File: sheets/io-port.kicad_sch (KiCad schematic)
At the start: 3 parts, among them J2 Conn_02x05_Odd_Even, U8 PCF8574AT

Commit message: add mcu module + position components
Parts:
- SW2: value ~ -> TDS08SGRNTU04; footprint (none) -> Connectors:TDS08SGRNTU04; LCSC (none) -> C6284382
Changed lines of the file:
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@@
 		(on_board yes)
 		(dnp no)
-		(property "Reference" "#PWR042"
+		(property "Reference" "#PWR043"
 			(at 203.2 53.34 0)
 			(effects
@@
 			(project "esp32-didatic-kit"
 				(path "/f57920a5-fee7-4fe5-a133-e8b36941a5a6/9698fb71-dcf7-48f9-beeb-6e6a219382b5/5496c104-71a9-407f-b983-09bd756c4ea4"
-					(reference "#PWR076")
-					(unit 1)
-				)
-				(path "/f57920a5-fee7-4fe5-a133-e8b36941a5a6/9698fb71-dcf7-48f9-beeb-6e6a219382b5/6574d7d9-6af9-409e-b5ea-1bf318741d30"
-					(reference "#PWR070")
-					(unit 1)
-				)
-				(path "/f57920a5-fee7-4fe5-a133-e8b36941a5a6/9698fb71-dcf7-48f9-beeb-6e6a219382b5/8379860e-8981-4170-acaa-d64afdf257d5"
-					(reference "#PWR042")
-					(unit 1)
-				)
-				(path "/f57920a5-fee7-4fe5-a133-e8b36941a5a6/9698fb71-dcf7-48f9-beeb-6e6a219382b5/ecc54a16-e833-4b48-9402-1bdf868c1d08"
-					(reference "#PWR064")
+					(reference "#PWR077")
+					(unit 1)
+				)
+				(path "/f57920a5-fee7-4fe5-a133-e8b36941a5a6/9698fb71-dcf7-48f9-beeb-6e6a219382b5/6574d7d9-6af9-409e-b5ea-1bf318741d30"
+					(reference "#PWR071")
+					(unit 1)
+				)
+				(path "/f57920a5-fee7-4fe5-a133-e8b36941a5a6/9698fb71-dcf7-48f9-beeb-6e6a219382b5/8379860e-8981-4170-acaa-d64afdf257d5"
+					(reference "#PWR043")
+					(unit 1)
+				)
+				(path "/f57920a5-fee7-4fe5-a133-e8b36941a5a6/9698fb71-dcf7-48f9-beeb-6e6a219382b5/ecc54a16-e833-4b48-9402-1bdf868c1d08"
+					(reference "#PWR065")
 					(unit 1)
 				)
@@
 		(dnp no)
 		(fields_autoplaced yes)
-		(property "Reference" "#PWR041"
+		(property "Reference" "#PWR042"
 			(at 153.67 91.44 0)
 			(effects
@@
 			(project "esp32-didatic-kit"
 				(path "/f57920a5-fee7-4fe5-a133-e8b36941a5a6/9698fb71-dcf7-48f9-beeb-6e6a219382b5/5496c104-71a9-407f-b983-09bd756c4ea4"
-					(reference "#PWR075")
-					(unit 1)
-				)
-				(path "/f57920a5-fee7-4fe5-a133-e8b36941a5a6/9698fb71-dcf7-48f9-beeb-6e6a219382b5/6574d7d9-6af9-409e-b5ea-1bf318741d30"
-					(reference "#PWR069")
-					(unit 1)
-				)
-				(path "/f57920a5-fee7-4fe5-a133-e8b36941a5a6/9698fb71-dcf7-48f9-beeb-6e6a219382b5/8379860e-8981-4170-acaa-d64afdf257d5"
-					(reference "#PWR041")
-					(unit 1)
-				)
-				(path "/f57920a5-fee7-4fe5-a133-e8b36941a5a6/9698fb71-dcf7-48f9-beeb-6e6a219382b5/ecc54a16-e833-4b48-9402-1bdf868c1d08"
-					(reference "#PWR063")
+					(reference "#PWR076")
+					(unit 1)
+				)
+				(path "/f57920a5-fee7-4fe5-a133-e8b36941a5a6/9698fb71-dcf7-48f9-beeb-6e6a219382b5/6574d7d9-6af9-409e-b5ea-1bf318741d30"
+					(reference "#PWR070")
+					(unit 1)
+				)
+				(path "/f57920a5-fee7-4fe5-a133-e8b36941a5a6/9698fb71-dcf7-48f9-beeb-6e6a219382b5/8379860e-8981-4170-acaa-d64afdf257d5"
+					(reference "#PWR042")
+					(unit 1)
+				)
+				(path "/f57920a5-fee7-4fe5-a133-e8b36941a5a6/9698fb71-dcf7-48f9-beeb-6e6a219382b5/ecc54a16-e833-4b48-9402-1bdf868c1d08"
+					(reference "#PWR064")
 					(unit 1)
 				)
@@
 		(dnp no)
 		(fields_autoplaced yes)
-		(property "Reference" "#PWR043"
+		(property "Reference" "#PWR044"
 			(at 203.2 104.14 0)
 			(effects
@@
 			(project "esp32-didatic-kit"
 				(path "/f57920a5-fee7-4fe5-a133-e8b36941a5a6/9698fb71-dcf7-48f9-beeb-6e6a219382b5/5496c104-71a9-407f-b983-09bd756c4ea4"
-					(reference "#PWR077")
-					(unit 1)
-				)
-				(path "/f57920a5-fee7-4fe5-a133-e8b36941a5a6/9698fb71-dcf7-48f9-beeb-6e6a219382b5/6574d7d9-6af9-409e-b5ea-1bf318741d30"
-					(reference "#PWR071")
-					(unit 1)
-				)
-				(path "/f57920a5-fee7-4fe5-a133-e8b36941a5a6/9698fb71-dcf7-48f9-beeb-6e6a219382b5/8379860e-8981-4170-acaa-d64afdf257d5"
-					(reference "#PWR043")
-					(unit 1)
-				)
-				(path "/f57920a5-fee7-4fe5-a133-e8b36941a5a6/9698fb71-dcf7-48f9-beeb-6e6a219382b5/ecc54a16-e833-4b48-9402-1bdf868c1d08"
-					(reference "#PWR065")
+					(reference "#PWR078")
+					(unit 1)
+				)
+				(path "/f57920a5-fee7-4fe5-a133-e8b36941a5a6/9698fb71-dcf7-48f9-beeb-6e6a219382b5/6574d7d9-6af9-409e-b5ea-1bf318741d30"
+					(reference "#PWR072")
+					(unit 1)
+				)
+				(path "/f57920a5-fee7-4fe5-a133-e8b36941a5a6/9698fb71-dcf7-48f9-beeb-6e6a219382b5/8379860e-8981-4170-acaa-d64afdf257d5"
+					(reference "#PWR044")
+					(unit 1)
+				)
+				(path "/f57920a5-fee7-4fe5-a133-e8b36941a5a6/9698fb71-dcf7-48f9-beeb-6e6a219382b5/ecc54a16-e833-4b48-9402-1bdf868c1d08"
+					(reference "#PWR066")
 					(unit 1)
 				)
@@
 		(on_board yes)
 		(dnp no)
-		(property "Reference" "#PWR040"
+		(property "Reference" "#PWR041"
 			(at 127 80.01 0)
 			(effects
@@
 			(project "esp32-didatic-kit"
 				(path "/f57920a5-fee7-4fe5-a133-e8b36941a5a6/9698fb71-dcf7-48f9-beeb-6e6a219382b5/5496c104-71a9-407f-b983-09bd756c4ea4"
-					(reference "#PWR074")
-					(unit 1)
-				)
-				(path "/f57920a5-fee7-4fe5-a133-e8b36941a5a6/9698fb71-dcf7-48f9-beeb-6e6a219382b5/6574d7d9-6af9-409e-b5ea-1bf318741d30"
-					(reference "#PWR068")
-					(unit 1)
-				)
-				(path "/f57920a5-fee7-4fe5-a133-e8b36941a5a6/9698fb71-dcf7-48f9-beeb-6e6a219382b5/8379860e-8981-4170-acaa-d64afdf257d5"
-					(reference "#PWR040")
-					(unit 1)
-				)
-				(path "/f57920a5-fee7-4fe5-a133-e8b36941a5a6/9698fb71-dcf7-48f9-beeb-6e6a219382b5/ecc54a16-e833-4b48-9402-1bdf868c1d08"
-					(reference "#PWR062")
+					(reference "#PWR075")
+					(unit 1)
+				)
+				(path "/f57920a5-fee7-4fe5-a133-e8b36941a5a6/9698fb71-dcf7-48f9-beeb-6e6a219382b5/6574d7d9-6af9-409e-b5ea-1bf318741d30"
+					(reference "#PWR069")
+					(unit 1)
+				)
+				(path "/f57920a5-fee7-4fe5-a133-e8b36941a5a6/9698fb71-dcf7-48f9-beeb-6e6a219382b5/8379860e-8981-4170-acaa-d64afdf257d5"
+					(reference "#PWR041")
+					(unit 1)
+				)
+				(path "/f57920a5-fee7-4fe5-a133-e8b36941a5a6/9698fb71-dcf7-48f9-beeb-6e6a219382b5/ecc54a16-e833-4b48-9402-1bdf868c1d08"
+					(reference "#PWR063")
 					(unit 1)
 				)
@@
 			)
 		)
-		(property "Value" "~"
+		(property "Value" "TDS08SGRNTU04"
 			(at 194.31 52.705 0)
 			(effects
@@
 			)
 		)
-		(property "Footprint" ""
+		(property "Footprint" "Connectors:TDS08SGRNTU04"
 			(at 193.675 78.105 0)
 			(effects
@@
 		)
 		(property "Description" ""
+			(at 193.675 78.105 0)
+			(effects
+				(font
+					(size 1.27 1.27)
+				)
+				(hide yes)
+			)
+		)
+		(property "LCSC" "C6284382"
 			(at 193.675 78.105 0)
 			(effects
@@
 		(dnp no)
 		(fields_autoplaced yes)
-		(property "Reference" "#PWR039"
+		(property "Reference" "#PWR040"
 			(at 91.44 102.87 0)
 			(effects
@@
 			(project "esp32-didatic-kit"
 				(path "/f57920a5-fee7-4fe5-a133-e8b36941a5a6/9698fb71-dcf7-48f9-beeb-6e6a219382b5/5496c104-71a9-407f-b983-09bd756c4ea4"
-					(reference "#PWR073")
-					(unit 1)
-				)
-				(path "/f57920a5-fee7-4fe5-a133-e8b36941a5a6/9698fb71-dcf7-48f9-beeb-6e6a219382b5/6574d7d9-6af9-409e-b5ea-1bf318741d30"
-					(reference "#PWR067")
-					(unit 1)
-				)
-				(path "/f57920a5-fee7-4fe5-a133-e8b36941a5a6/9698fb71-dcf7-48f9-beeb-6e6a219382b5/8379860e-8981-4170-acaa-d64afdf257d5"
-					(reference "#PWR039")
-					(unit 1)
-				)
-				(path "/f57920a5-fee7-4fe5-a133-e8b36941a5a6/9698fb71-dcf7-48f9-beeb-6e6a219382b5/ecc54a16-e833-4b48-9402-1bdf868c1d08"
-					(reference "#PWR061")
+					(reference "#PWR074")
+					(unit 1)
+				)
+				(path "/f57920a5-fee7-4fe5-a133-e8b36941a5a6/9698fb71-dcf7-48f9-beeb-6e6a219382b5/6574d7d9-6af9-409e-b5ea-1bf318741d30"
+					(reference "#PWR068")
+					(unit 1)
+				)
+				(path "/f57920a5-fee7-4fe5-a133-e8b36941a5a6/9698fb71-dcf7-48f9-beeb-6e6a219382b5/8379860e-8981-4170-acaa-d64afdf257d5"
+					(reference "#PWR040")
+					(unit 1)
+				)
+				(path "/f57920a5-fee7-4fe5-a133-e8b36941a5a6/9698fb71-dcf7-48f9-beeb-6e6a219382b5/ecc54a16-e833-4b48-9402-1bdf868c1d08"
+					(reference "#PWR062")
 					(unit 1)
 				)
@@
 		(on_board yes)
 		(dnp no)
-		(property "Reference" "#PWR038"
+		(property "Reference" "#PWR039"
 			(at 91.44 52.07 0)
 			(effects
@@
 			(project "esp32-didatic-kit"
 				(path "/f57920a5-fee7-4fe5-a133-e8b36941a5a6/9698fb71-dcf7-48f9-beeb-6e6a219382b5/5496c104-71a9-407f-b983-09bd756c4ea4"
-					(reference "#PWR072")
-					(unit 1)
-				)
-				(path "/f57920a5-fee7-4fe5-a133-e8b36941a5a6/9698fb71-dcf7-48f9-beeb-6e6a219382b5/6574d7d9-6af9-409e-b5ea-1bf318741d30"
-					(reference "#PWR066")
-					(unit 1)
-				)
-				(path "/f57920a5-fee7-4fe5-a133-e8b36941a5a6/9698fb71-dcf7-48f9-beeb-6e6a219382b5/8379860e-8981-4170-acaa-d64afdf257d5"
-					(reference "#PWR038")
-					(unit 1)
-				)
-				(path "/f57920a5-fee7-4fe5-a133-e8b36941a5a6/9698fb71-dcf7-48f9-beeb-6e6a219382b5/ecc54a16-e833-4b48-9402-1bdf868c1d08"
-					(reference "#PWR060")
-					(unit 1)
-				)
+					(reference "#PWR073")
+					(unit 1)
+				)
+				(path "/f57920a5-fee7-4fe5-a133-e8b36941a5a6/9698fb71-dcf7-48f9-beeb-6e6a219382b5/6574d7d9-6af9-409e-b5ea-1bf318741d30"
+					(reference "#PWR067")
+					(unit 1)
+				)
+				(path "/f57920a5-fee7-4fe5-a133-e8b36941a5a6/9698fb71-dcf7-48f9-beeb-6e6a219382b5/8379860e-8981-4170-acaa-d64afdf257d5"
+					(reference "#PWR039")
+					(unit 1)
+				)
+				(path "/f57920a5-fee7-4fe5-a133-e8b36941a5a6/9698fb71-dcf7-48f9-beeb-6e6a219382b5/ecc54a16-e833-4b48-9402-1bdf868c1d08"
+					(reference "#PWR061")
+					(unit 1)
+				)

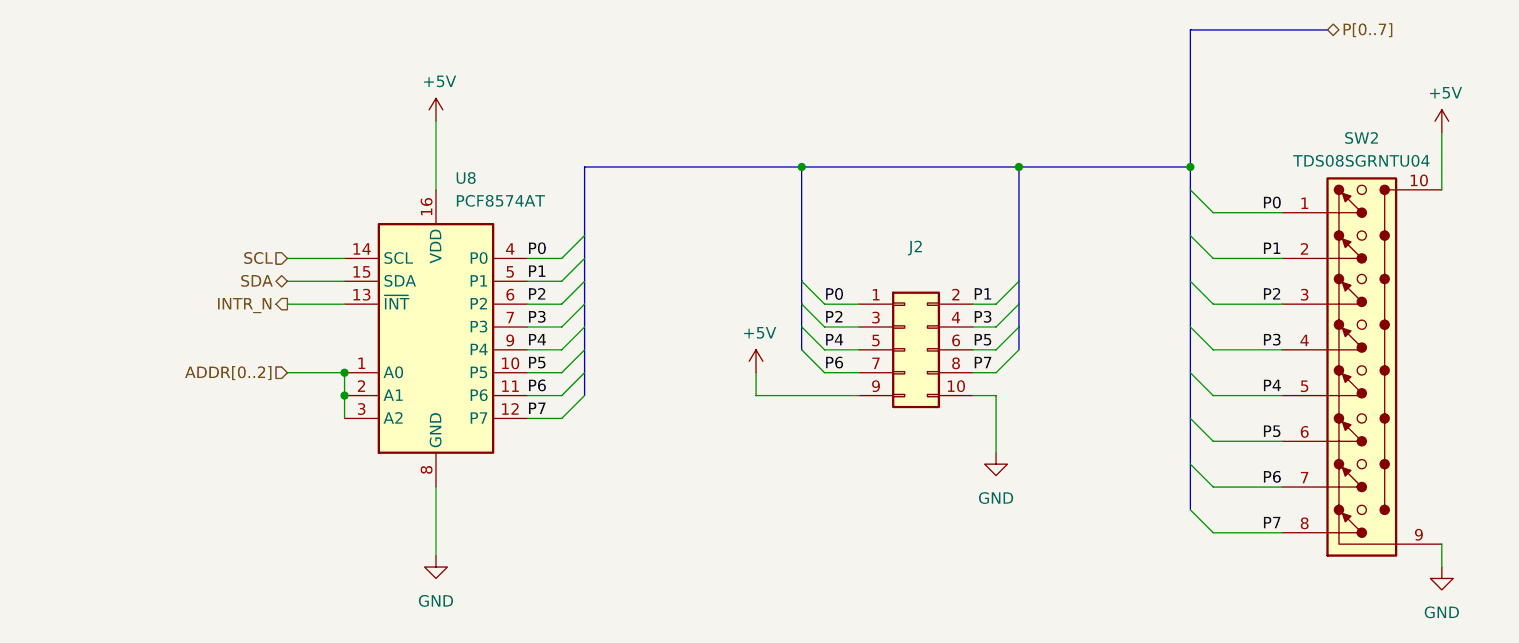
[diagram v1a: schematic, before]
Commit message: add PA an PB ports
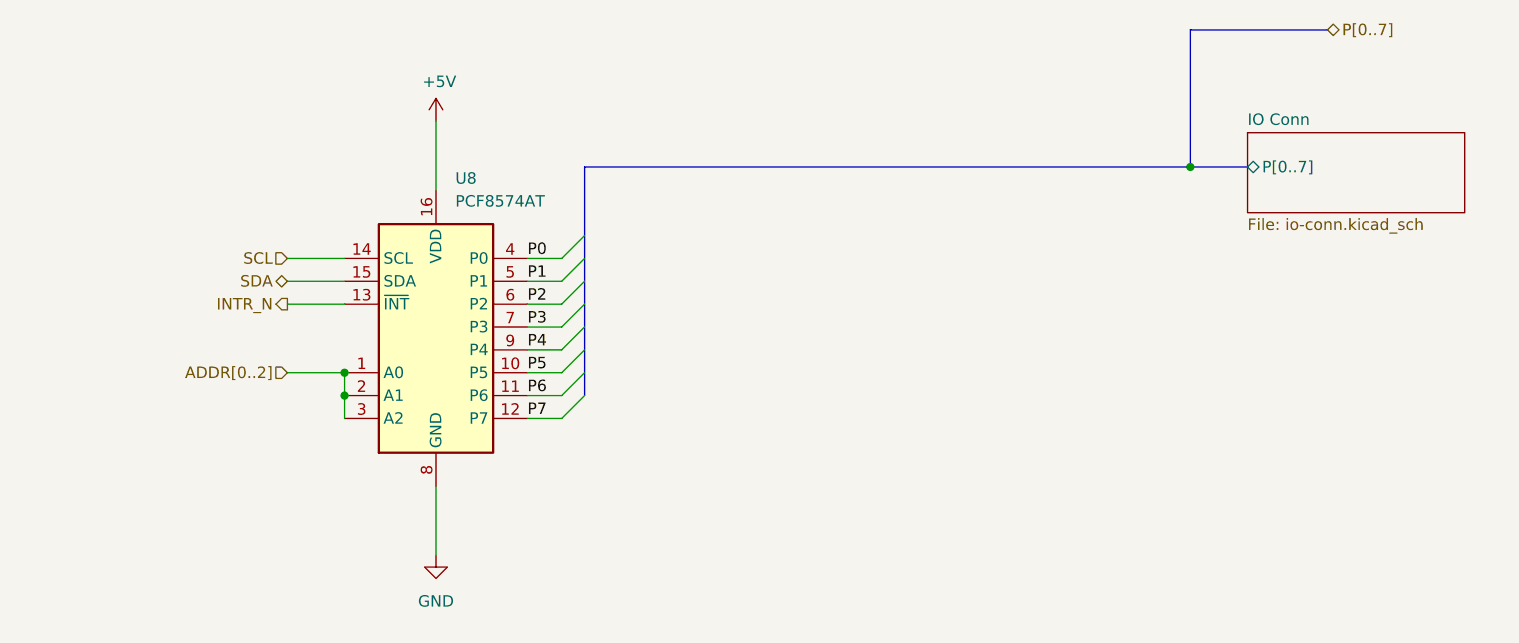
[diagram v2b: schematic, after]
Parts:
- removed J2: Conn_02x05_Odd_Even, Connector_PinHeader_2.54mm:PinHeader_2x05_P2.54mm_Vertical, symbol Connector_Generic:Conn_02x05_Odd_Even
- removed SW2: TDS08SGRNTU04, Connectors:TDS08SGRNTU04, symbol Connectors:TRI-STATE_DIP_8P
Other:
- added sheet IO Conn (io-conn.kicad_sch)

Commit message: updated silk + started routing
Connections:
- net ADDR[0..2]: no longer U8.1 (A0), U8.2 (A1), U8.3 (A2)
- new net ADDR0: U8.1 (A0)
- new net ADDR1: U8.2 (A1)
- new net ADDR2: U8.3 (A2)
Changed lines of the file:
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@@
 	(paper "A4")
-	(junction
-		(at 81.28 78.74)
-		(diameter 0)
-		(color 0 0 0 0)
-	)
 	(junction
 		(at 175.26 53.34)
@@
 		(color 0 0 0 0)
 	)
-	(junction
-		(at 81.28 76.2)
-		(diameter 0)
-		(color 0 0 0 0)
-	)
 	(bus_entry
 		(at 107.95 60.96)
@@
 	)
 	(bus_entry
+		(at 71.12 73.66)
+		(size 2.54 2.54)
+		(stroke
+			(width 0)
+			(type default)
+		)
+	)
+	(bus_entry
 		(at 107.95 66.04)
 		(size -2.54 2.54)
@@
 	)
 	(bus_entry
+		(at 68.58 73.66)
+		(size 2.54 2.54)
+		(stroke
+			(width 0)
+			(type default)
+		)
+	)
+	(bus_entry
 		(at 107.95 76.2)
 		(size -2.54 2.54)
@@
 	)
 	(bus_entry
+		(at 66.04 73.66)
+		(size 2.54 2.54)
+		(stroke
+			(width 0)
+			(type default)
+		)
+	)
+	(bus_entry
 		(at 107.95 68.58)
 		(size -2.54 2.54)
@@
 		)
 	)
-	(wire
-		(pts
-			(xy 81.28 78.74) (xy 81.28 81.28)
-		)
-		(stroke
-			(width 0)
-			(type default)
-		)
-	)
 	(bus
 		(pts
@@
 		)
 	)
+	(wire
+		(pts
+			(xy 73.66 76.2) (xy 81.28 76.2)
+		)
+		(stroke
+			(width 0)
+			(type default)
+		)
+	)
 	(bus
 		(pts
@@
 		)
 	)
-	(wire
-		(pts
-			(xy 74.93 76.2) (xy 81.28 76.2)
-		)
-		(stroke
-			(width 0)
-			(type default)
-		)
-	)
 	(bus
 		(pts
@@
 		)
 	)
+	(bus
+		(pts
+			(xy 59.69 73.66) (xy 66.04 73.66)
+		)
+		(stroke
+			(width 0)
+			(type default)
+		)
+	)
+	(bus
+		(pts
+			(xy 66.04 73.66) (xy 68.58 73.66)
+		)
+		(stroke
+			(width 0)
+			(type default)
+		)
+	)
 	(wire
 		(pts
@@
 	(wire
 		(pts
+			(xy 71.12 76.2) (xy 71.12 78.74)
+		)
+		(stroke
+			(width 0)
+			(type default)
+		)
+	)
+	(wire
+		(pts
 			(xy 105.41 73.66) (xy 101.6 73.66)
 		)
@@
 	(wire
 		(pts
+			(xy 71.12 78.74) (xy 81.28 78.74)
+		)
+		(stroke
+			(width 0)
+			(type default)
+		)
+	)
+	(wire
+		(pts
 			(xy 105.41 81.28) (xy 101.6 81.28)
 		)
@@
 	(wire
 		(pts
-			(xy 81.28 76.2) (xy 81.28 78.74)
+			(xy 68.58 76.2) (xy 68.58 81.28)
 		)
 		(stroke
@@
 		(pts
 			(xy 74.93 66.04) (xy 81.28 66.04)
+		)
+		(stroke
+			(width 0)
+			(type default)
+		)
+	)
+	(bus
+		(pts
+			(xy 68.58 73.66) (xy 71.12 73.66)
+		)
+		(stroke
+			(width 0)
+			(type default)
+		)
+	)
+	(wire
+		(pts
+			(xy 68.58 81.28) (xy 81.28 81.28)
 		)
 		(stroke
@@
 		)
 	)
+	(label "ADDR0"
+		(at 73.66 76.2 0)
+		(effects
+			(font
+				(size 1.27 1.27)
+			)
+			(justify left bottom)
+		)
+	)
 	(label "P3"
 		(at 101.6 71.12 0)
@@
 		)
 	)
+	(label "ADDR1"
+		(at 73.66 78.74 0)
+		(effects
+			(font
+				(size 1.27 1.27)
+			)
+			(justify left bottom)
+		)
+	)
 	(label "P6"
 		(at 101.6 78.74 0)
+		(effects
+			(font
+				(size 1.27 1.27)
+			)
+			(justify left bottom)
+		)
+	)
+	(label "ADDR2"
+		(at 73.66 81.28 0)
 		(effects
 			(font
@@
 	(hierarchical_label "ADDR[0..2]"
 		(shape input)
-		(at 74.93 76.2 180)
-		(effects
-			(font
+		(at 59.69 73.66 180)
+		(effects
+			(font
